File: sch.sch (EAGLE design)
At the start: 13 parts

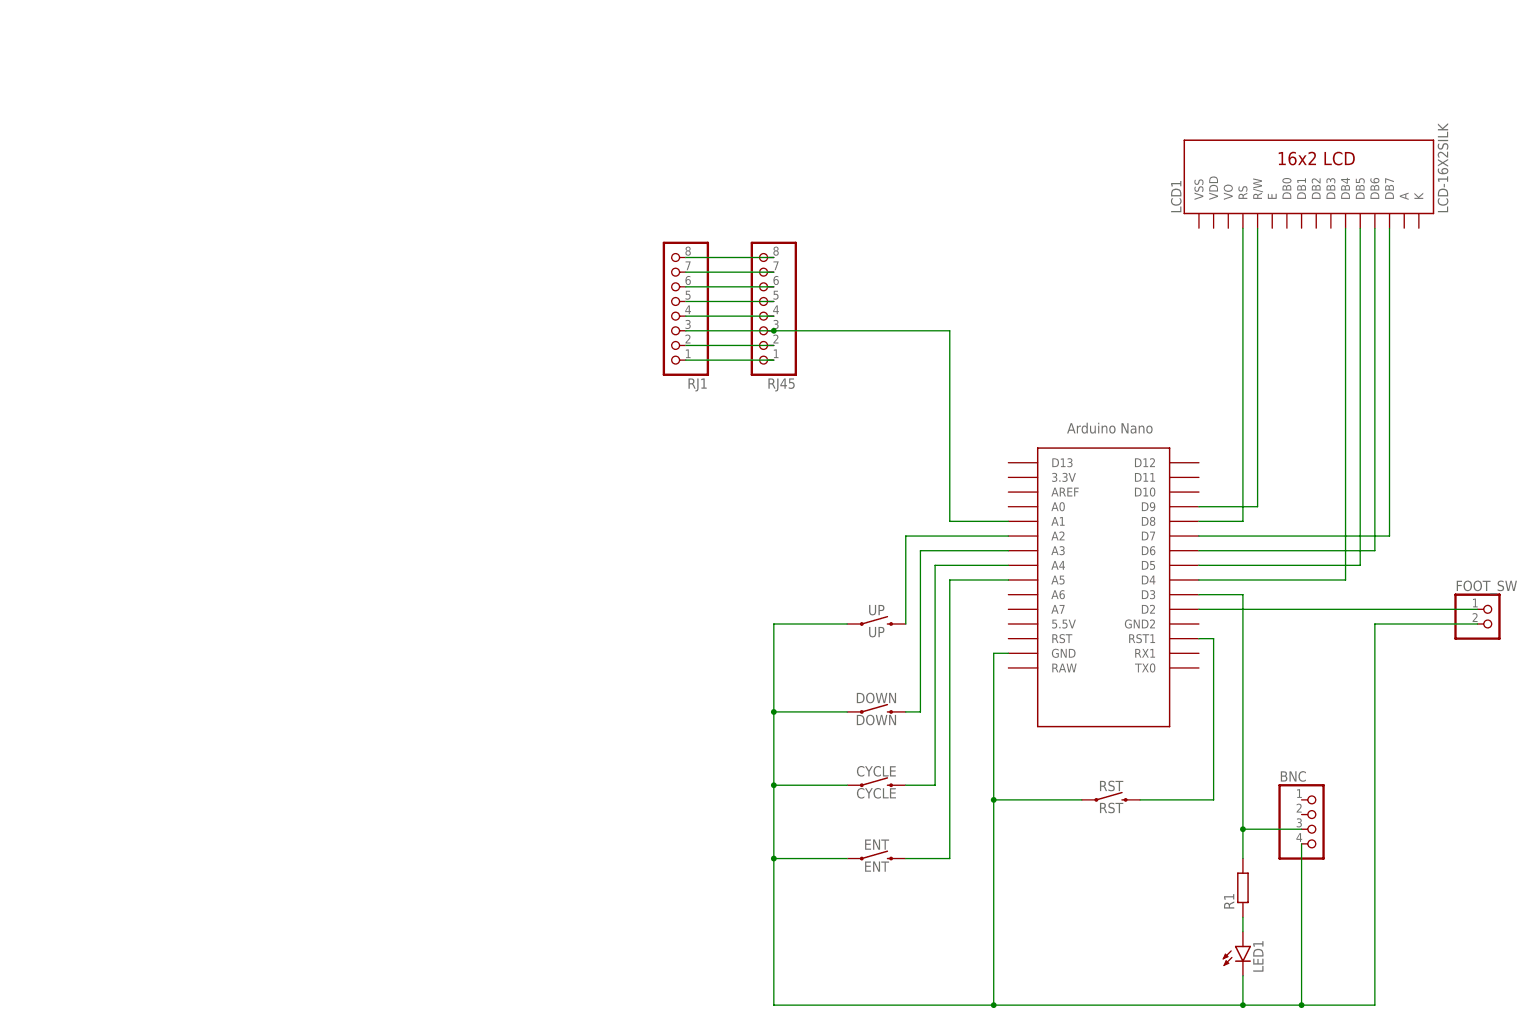
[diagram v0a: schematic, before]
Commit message: add rj45
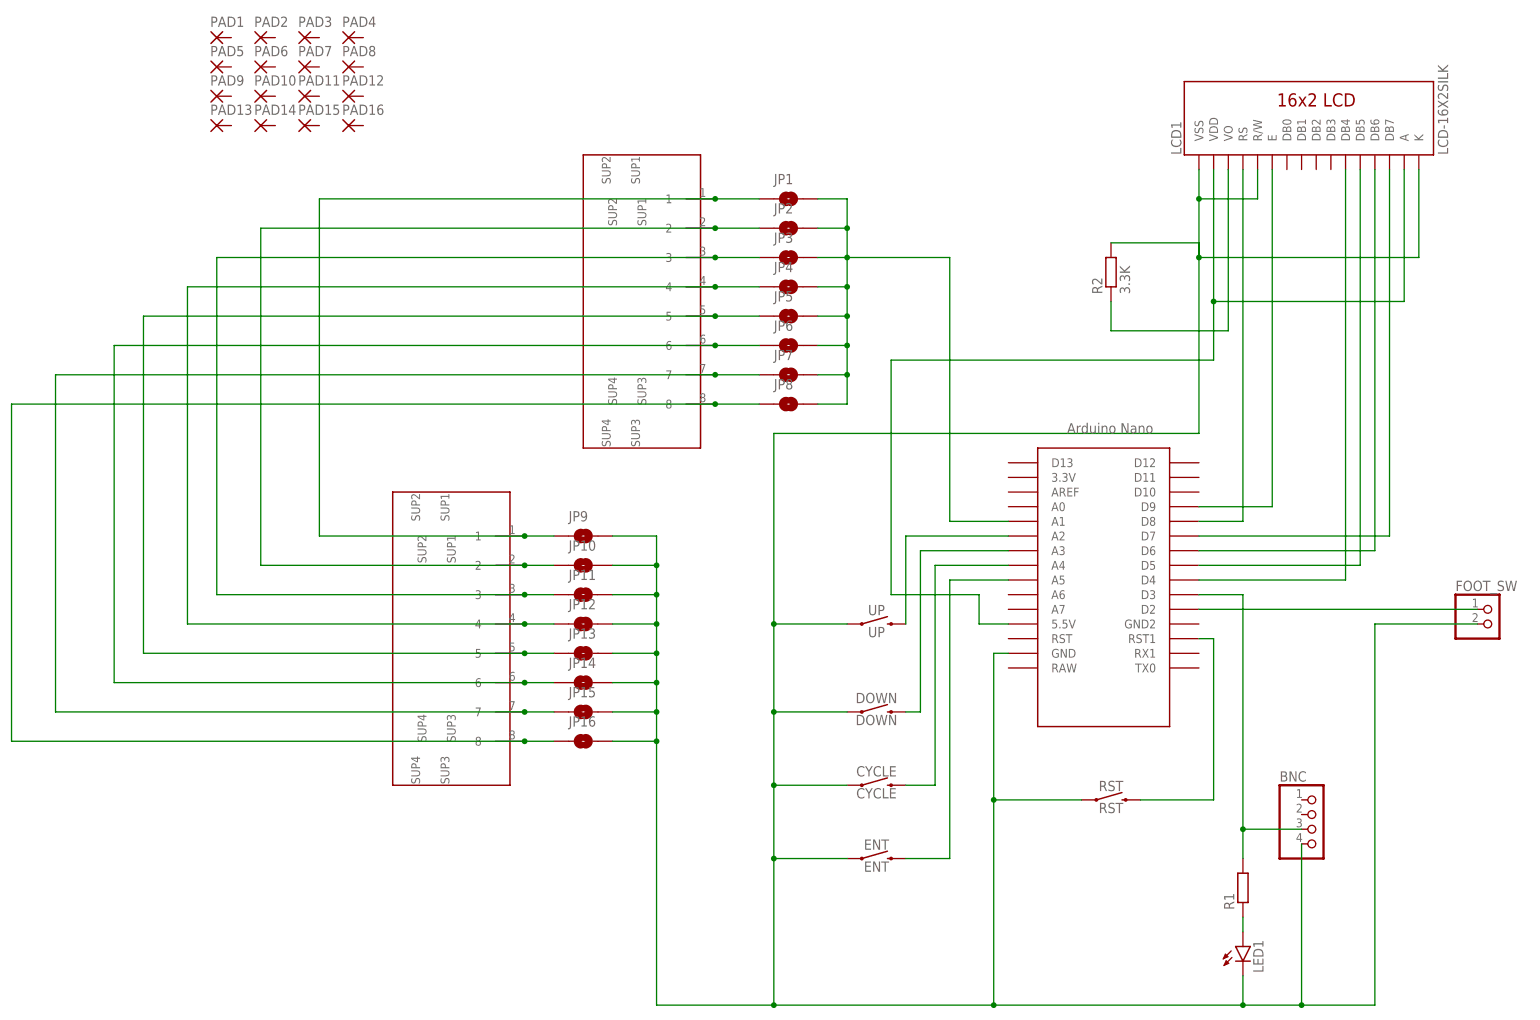
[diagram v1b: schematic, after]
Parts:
- removed RJ1, RJ45: (no value), pinhead:PINHD-1X8
- added JP1, JP10, JP11, JP12, JP13, JP14, JP15, JP16, JP2, JP3, JP4, JP5, JP6, JP7, JP8, JP9: JUMPER-SMT_2_NO_SILK, SparkFun-Jumpers:JUMPER-SMT_2_NO_SILK
- added LAN1, LAN2: RJ45, rj45:RJ45
- added PAD1, PAD10, PAD11, PAD12, PAD13, PAD14, PAD15, PAD16, PAD2, PAD3, PAD4, PAD5, PAD6, PAD7, PAD8, PAD9: (no value), wirepad:1,6/0,8
- added R2: 3.3K, resistor:R-EU_0207/7
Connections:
- removed net N$18: RJ1.7, RJ45.7
- new net N$24: JP15.1, JP7.1, LAN1.7, LAN2.7
- new net N$25: JP16.1, JP8.1, LAN1.8, LAN2.8
- new net N$26: JP1.1, JP9.1, LAN1.1, LAN2.1
- new net N$36: LCD1.VO, R2.1
- net N$10: now also JP1.2, JP2.2, JP3.2, JP4.2, JP5.2, JP6.2, JP7.2, JP8.2; no longer RJ1.3, RJ45.3
- net N$12: now also LCD1.A, LCD1.VDD, U$1.5.5V; no longer BNC.4, CYCLE.1, DOWN.1, ENT.1, FOOT_SW.2, LED1.C, RST.1, U$1.GND, UP.1
- net N$16: now also BNC.4, CYCLE.1, DOWN.1, ENT.1, FOOT_SW.2, JP10.2, JP11.2, JP12.2, JP13.2, JP14.2, JP15.2, JP16.2, JP9.2, LCD1.K, LCD1.R/W, LCD1.VSS, LED1.C, R2.2, RST.1, U$1.GND, UP.1; no longer RJ1.8, RJ45.8
- net N$19: now also JP10.1, JP2.1, LAN1.2, LAN2.2; no longer RJ1.6, RJ45.6
- net N$2: now also LCD1.E; no longer LCD1.R/W
- net N$20: now also JP11.1, JP3.1, LAN1.3, LAN2.3; no longer RJ1.5, RJ45.5
- net N$21: now also JP12.1, JP4.1, LAN1.4, LAN2.4; no longer RJ1.4, RJ45.4
- net N$22: now also JP13.1, JP5.1, LAN1.5, LAN2.5; no longer RJ1.2, RJ45.2
- net N$23: now also JP14.1, JP6.1, LAN1.6, LAN2.6; no longer RJ1.1, RJ45.1
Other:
- moved on the sheet: LCD1
